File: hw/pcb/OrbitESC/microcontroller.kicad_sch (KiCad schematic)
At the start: 45 parts, among them J6 CAN1, J7 Serial1, U1 TLE9250X, U2 AT25SF081-SSHD-X, U3 24LC128

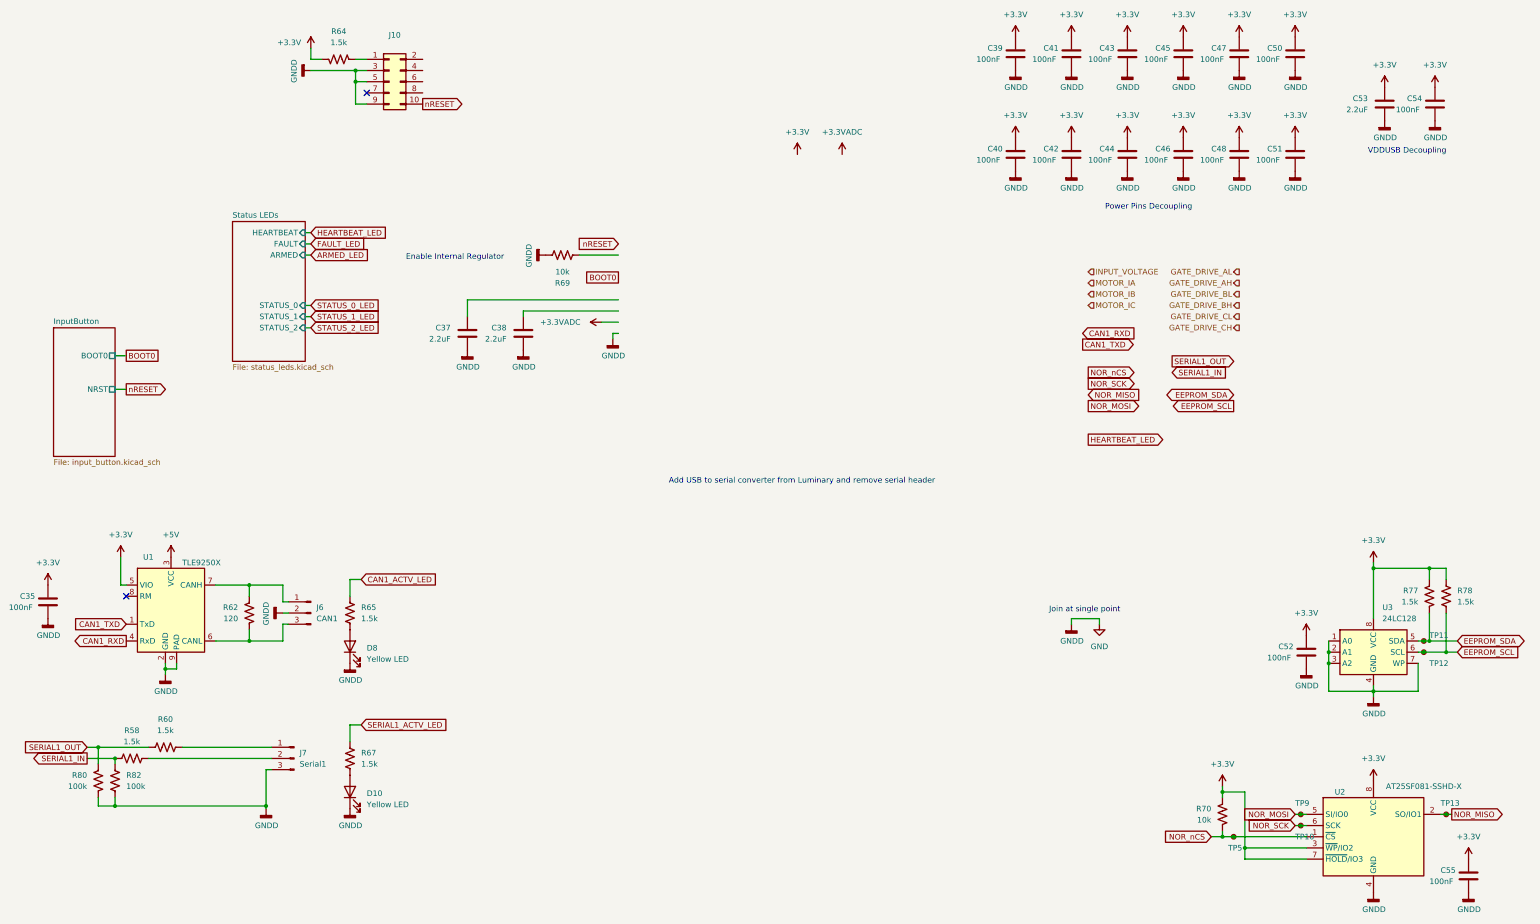
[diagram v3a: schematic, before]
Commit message: Rework new processor
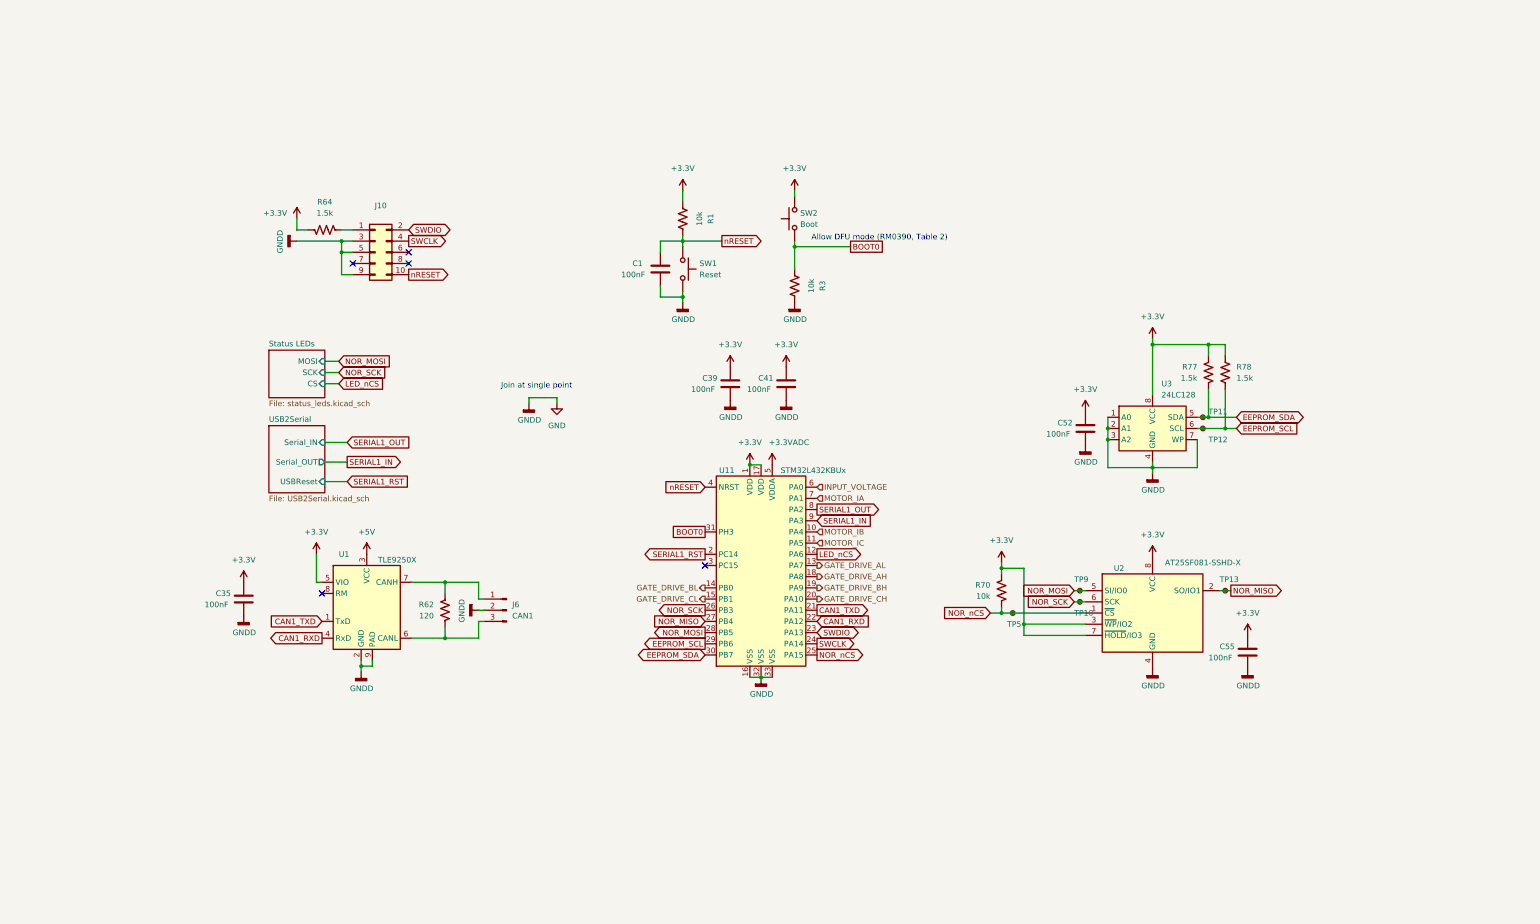
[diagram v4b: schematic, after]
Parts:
- removed C37, C38, C53: 2.2uF, Capacitor_SMD:C_0805_2012Metric, symbol Device:C
- removed C40, C42, C43, C44, C45, C46, C47, C48, C50, C51, C54: 100nF, Capacitor_SMD:C_0402_1005Metric, symbol Device:C
- removed D10, D8: Yellow LED, Diode_SMD:D_0603_1608Metric, symbol Device:LED
- removed J7: Serial1, Connector_JST:JST_PH_B3B-PH-K_1x03_P2.00mm_Vertical, symbol Connector:Conn_01x03_Male
- removed R58, R60, R65, R67: 1.5k, Resistor_SMD:R_0402_1005Metric, symbol Device:R_US
- removed R69: 10k, Resistor_SMD:R_0402_1005Metric, symbol Device:R_US
- removed R80, R82: 100k, Resistor_SMD:R_0402_1005Metric, symbol Device:R_US
- added C1: 100nF, Capacitor_SMD:C_0402_1005Metric, symbol Device:C
- added R1, R3: 10k, Resistor_SMD:R_0402_1005Metric, symbol Device:R_US
- added SW1: Reset, Button_Switch_SMD:SW_SPST_PTS810, symbol Switch:SW_Push
- added SW2: Boot, Button_Switch_SMD:SW_SPST_PTS810, symbol Switch:SW_Push
- added U11: STM32L432KBUx, Package_DFN_QFN:QFN-32-1EP_5x5mm_P0.5mm_EP3.45x3.45mm, symbol MCU_ST_STM32L4:STM32L432KBUx
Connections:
- net +3.3V: now also R1.2, SW2.2, U11.1 (VDD), U11.17 (VDD)
- net +3.3VADC: now also U11.5 (VDDA)
- net BOOT0: now also R3.2, SW2.1, U11.31 (PH3)
- net CAN1_RXD: now also U11.22 (PA12)
- net CAN1_TXD: now also U11.21 (PA11)
- net EEPROM_SCL: now also U11.29 (PB6)
- net EEPROM_SDA: now also U11.30 (PB7)
- net GATE_DRIVE_AH: now also U11.18 (PA8)
- net GATE_DRIVE_AL: now also U11.13 (PA7)
- net GATE_DRIVE_BH: now also U11.19 (PA9)
- net GATE_DRIVE_BL: now also U11.14 (PB0)
- net GATE_DRIVE_CH: now also U11.20 (PA10)
- net GATE_DRIVE_CL: now also U11.15 (PB1)
- net GND: now also C1.1, R3.1, SW1.2, U11.16 (VSS), U11.32 (VSS), U11.33 (VSS)
- net INPUT_VOLTAGE: now also U11.6 (PA0)
- net MOTOR_IA: now also U11.7 (PA1)
- net MOTOR_IB: now also U11.10 (PA4)
- net MOTOR_IC: now also U11.11 (PA5)
- net NOR_MISO: now also U11.27 (PB4)
- net NOR_MOSI: now also U11.28 (PB5)
- net NOR_SCK: now also U11.26 (PB3)
- net NOR_nCS: now also U11.25 (PA15)
- net SERIAL1_IN: now also U11.9 (PA3)
- net SERIAL1_OUT: now also U11.8 (PA2)
- net nRESET: now also C1.2, R1.1, SW1.1, U11.4 (NRST)
- net SWDIO: now reaches J10.2 (Pin_2)
- net SWDIO: now also U11.23 (PA13)
- net SWCLK: now reaches J10.4 (Pin_4)
- net SWCLK: now also U11.24 (PA14)
- new net LED_nCS: U11.12 (PA6)
- new net SERIAL1_RST: U11.2 (PC14)
- no-connect marks 2 -> 5
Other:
- removed sheet InputButton
- added sheet USB2Serial (USB2Serial.kicad_sch)
- sheet Status LEDs ports: added CS, MOSI, SCK; removed ARMED, FAULT, HEARTBEAT, STATUS_0, STATUS_1, STATUS_2
- note added: "Allow DFU mode (RM0390, Table 2)"
- note removed: "Add USB to serial converter from Luminary and remove serial header"
- note removed: "Enable Internal Regulator"
- note removed: "Power Pins Decoupling"
- note removed: "VDDUSB Decoupling"
- moved on the sheet: C35, C39, C41, C52, C55, J10, J6, R62, R64, R70, R77, R78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

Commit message: PCB cleanup
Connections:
- net GATE_DRIVE_AH: now also U11.20 (PA10); no longer U11.18 (PA8)
- net GATE_DRIVE_AL: now also U11.15 (PB1); no longer U11.13 (PA7)
- net GATE_DRIVE_CH: now also U11.18 (PA8); no longer U11.20 (PA10)
- net GATE_DRIVE_CL: now also U11.13 (PA7); no longer U11.15 (PB1)
- net MOTOR_IA: now also U11.10 (PA4); no longer U11.7 (PA1)
- net MOTOR_IB: now also U11.11 (PA5); no longer U11.10 (PA4)
- net MOTOR_IC: now also U11.7 (PA1); no longer U11.11 (PA5)
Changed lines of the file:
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@@
     )
   )
-  (hierarchical_label "GATE_DRIVE_CH" (shape output) (at 211.455 154.305 0)
+  (hierarchical_label "GATE_DRIVE_CH" (shape output) (at 211.455 149.225 0)
     (effects (font (size 1.27 1.27)) (justify left))
   )
-  (hierarchical_label "MOTOR_IB" (shape input) (at 211.455 139.065 0)
+  (hierarchical_label "MOTOR_IB" (shape input) (at 211.455 141.605 0)
     (effects (font (size 1.27 1.27)) (justify left))
   )
@@
     (effects (font (size 1.27 1.27)) (justify left))
   )
-  (hierarchical_label "GATE_DRIVE_AL" (shape output) (at 211.455 146.685 0)
+  (hierarchical_label "GATE_DRIVE_AL" (shape output) (at 186.055 154.305 180)
+    (effects (font (size 1.27 1.27)) (justify right))
+  )
+  (hierarchical_label "GATE_DRIVE_CL" (shape output) (at 211.455 146.685 0)
     (effects (font (size 1.27 1.27)) (justify left))
   )
-  (hierarchical_label "GATE_DRIVE_CL" (shape output) (at 186.055 154.305 180)
-    (effects (font (size 1.27 1.27)) (justify right))
-  )
-  (hierarchical_label "MOTOR_IC" (shape input) (at 211.455 141.605 0)
+  (hierarchical_label "MOTOR_IC" (shape input) (at 211.455 131.445 0)
     (effects (font (size 1.27 1.27)) (justify left))
   )
-  (hierarchical_label "MOTOR_IA" (shape input) (at 211.455 131.445 0)
+  (hierarchical_label "MOTOR_IA" (shape input) (at 211.455 139.065 0)
     (effects (font (size 1.27 1.27)) (justify left))
   )
@@
     (effects (font (size 1.27 1.27)) (justify left))
   )
-  (hierarchical_label "GATE_DRIVE_AH" (shape output) (at 211.455 149.225 0)
+  (hierarchical_label "GATE_DRIVE_AH" (shape output) (at 211.455 154.305 0)
     (effects (font (size 1.27 1.27)) (justify left))
   )

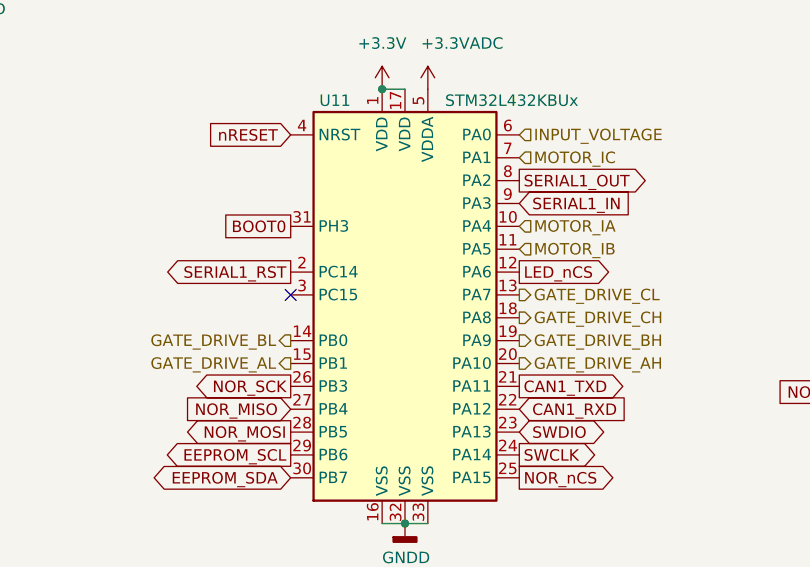
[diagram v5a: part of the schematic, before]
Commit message: First draft of routed PCB
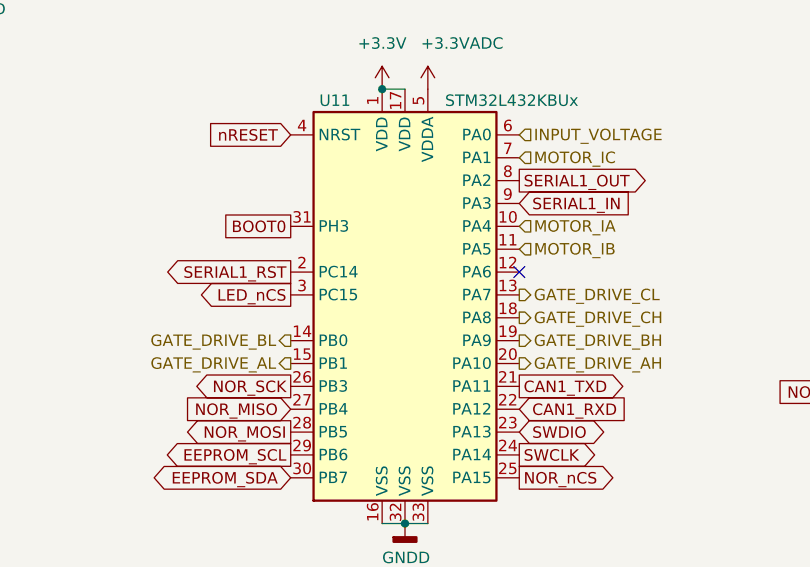
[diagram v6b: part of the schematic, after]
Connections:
- net LED_nCS: now also U11.3 (PC15); no longer U11.12 (PA6)
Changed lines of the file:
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@@
   )
   (no_connect (at 99.06 153.035))
+  (no_connect (at 211.455 144.145))
   (no_connect (at 118.745 78.105))
   (no_connect (at 118.745 75.565))
   (no_connect (at 106.045 78.105))
-  (no_connect (at 186.055 146.685))
   (wire (pts (xy 99.695 102.87) (xy 102.87 102.87))
     (stroke (width 0) (type default) (color 0 0 0 0))
@@
     )
   )
-  (global_label "LED_nCS" (shape output) (at 211.455 144.145 0) (fields_autoplaced)
-    (effects (font (size 1.27 1.27)) (justify left))
-    (property "Intersheet References" "${INTERSHEET_REFS}" (id 0) (at 221.9114 144.0656 0)
-      (effects (font (size 1.27 1.27)) (justify left) hide)
-    )
-  )
+  (global_label "LED_nCS" (shape output) (at 186.055 146.685 180) (fields_autoplaced)
+    (effects (font (size 1.27 1.27)) (justify right))
+    (property "Intersheet References" "${INTERSHEET_REFS}" (id 0) (at 175.5986 146.7644 0)
+      (effects (font (size 1.27 1.27)) (justify right) hide)
+    )
+  )

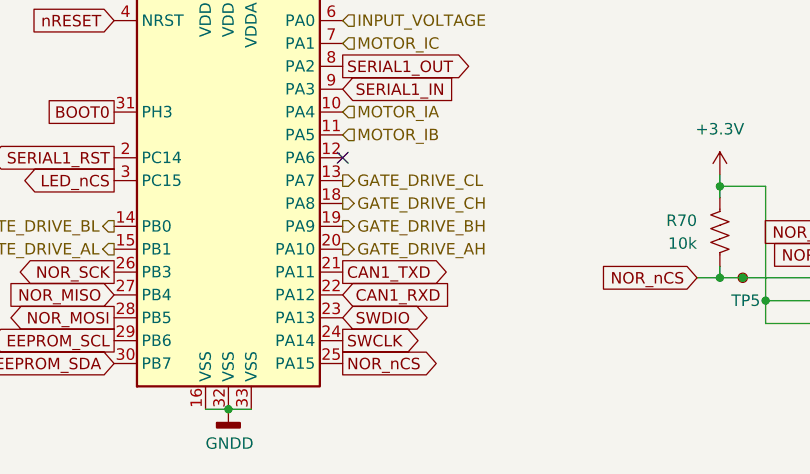
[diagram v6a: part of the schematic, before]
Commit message: Save a few board changes found when assembing PCB v1.0
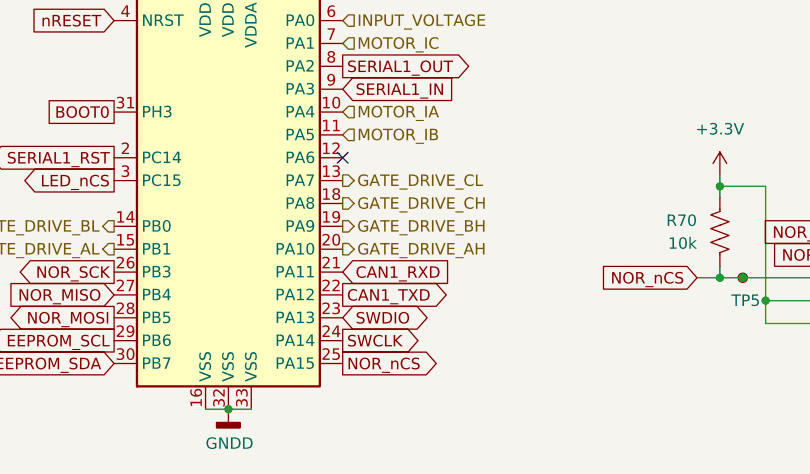
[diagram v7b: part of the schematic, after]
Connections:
- net CAN1_RXD: now also U11.21 (PA11); no longer U11.22 (PA12)
- net CAN1_TXD: now also U11.22 (PA12); no longer U11.21 (PA11)
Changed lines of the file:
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@@
     )
   )
-  (global_label "CAN1_TXD" (shape output) (at 211.455 156.845 0) (fields_autoplaced)
+  (global_label "CAN1_TXD" (shape output) (at 211.455 159.385 0) (fields_autoplaced)
     (effects (font (size 1.27 1.27)) (justify left))
-    (property "Intersheet References" "${INTERSHEET_REFS}" (id 0) (at 223.1814 156.9244 0)
+    (property "Intersheet References" "${INTERSHEET_REFS}" (id 0) (at 223.1814 159.4644 0)
       (effects (font (size 1.27 1.27)) (justify left) hide)
     )
@@
     )
   )
-  (global_label "CAN1_RXD" (shape input) (at 211.455 159.385 0) (fields_autoplaced)
+  (global_label "CAN1_RXD" (shape input) (at 211.455 156.845 0) (fields_autoplaced)
     (effects (font (size 1.27 1.27)) (justify left))
-    (property "Intersheet References" "${INTERSHEET_REFS}" (id 0) (at 223.4838 159.4644 0)
+    (property "Intersheet References" "${INTERSHEET_REFS}" (id 0) (at 223.4838 156.9244 0)
       (effects (font (size 1.27 1.27)) (justify left) hide)
     )

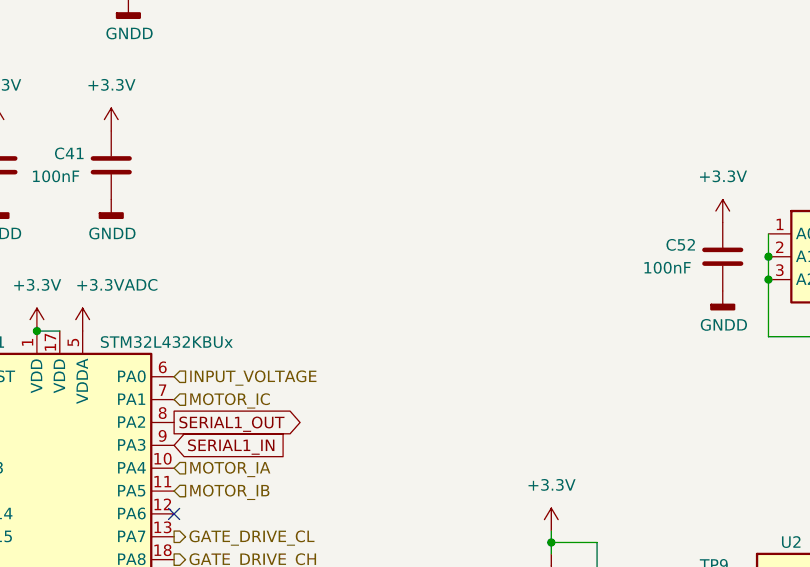
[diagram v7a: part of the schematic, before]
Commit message: Schematic corrections
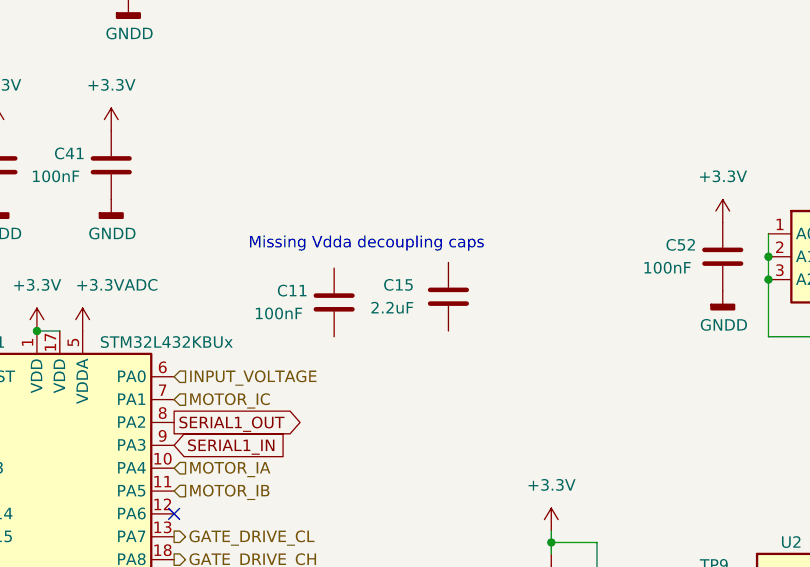
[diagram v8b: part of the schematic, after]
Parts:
- added C11: 100nF, Capacitor_SMD:C_0402_1005Metric, symbol Device:C
- added C15: 2.2uF, Capacitor_SMD:C_0805_2012Metric, symbol Device:C
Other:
- note added: "Missing Vdda decoupling caps"
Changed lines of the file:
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@@
     (stroke (width 0) (type default) (color 0 0 0 0))
+  )
+  (text "Missing Vdda decoupling caps" (at 219.71 114.935 0)
+    (effects (font (size 1.27 1.27)) (justify left bottom))
   )
   (text "Join at single point" (at 139.7 106.68 0)
@@
     (pin "2")
   )
+  (symbol (lib_id "Device:C") (at 229.235 120.65 180) (unit 1)
+    (in_bom yes) (on_board yes)
+    (property "Reference" "C11" (id 0) (at 222.885 119.38 0)
+      (effects (font (size 1.27 1.27)) (justify right))
+    )
+    (property "Value" "100nF" (id 1) (at 220.345 121.92 0)
+      (effects (font (size 1.27 1.27)) (justify right))
+    )
+    (property "Footprint" "Capacitor_SMD:C_0402_1005Metric" (id 2) (at 228.2698 116.84 0)
+      (effects (font (size 1.27 1.27)) hide)
+    )
+    (property "Datasheet" "~" (id 3) (at 229.235 120.65 0)
+      (effects (font (size 1.27 1.27)) hide)
+    )
+    (property "JLCPCB" "C307331" (id 4) (at 229.235 120.65 0)
+      (effects (font (size 1.27 1.27)) hide)
+    )
+    (pin "1")
+    (pin "2")
+  )
   (symbol (lib_id "Connector:TestPoint_Small") (at 299.085 113.03 0) (unit 1)
     (in_bom yes) (on_board yes)
@@
     (pin "1")
   )
+  (symbol (lib_id "Device:C") (at 241.935 120.015 0) (mirror x) (unit 1)
+    (in_bom yes) (on_board yes) (fields_autoplaced)
+    (property "Reference" "C15" (id 0) (at 238.125 118.7449 0)
+      (effects (font (size 1.27 1.27)) (justify right))
+    )
+    (property "Value" "2.2uF" (id 1) (at 238.125 121.2849 0)
+      (effects (font (size 1.27 1.27)) (justify right))
+    )
+    (property "Footprint" "Capacitor_SMD:C_0805_2012Metric" (id 2) (at 242.9002 116.205 0)
+      (effects (font (size 1.27 1.27)) hide)
+    )
+    (property "Datasheet" "~" (id 3) (at 241.935 120.015 0)
+      (effects (font (size 1.27 1.27)) hide)
+    )
+    (property "JLCPCB" "C49217" (id 4) (at 241.935 120.015 0)
+      (effects (font (size 1.27 1.27)) hide)
+    )
+    (pin "1")
+    (pin "2")
+  )
   (symbol (lib_id "power:+3.3VADC") (at 201.295 123.825 0) (unit 1)
